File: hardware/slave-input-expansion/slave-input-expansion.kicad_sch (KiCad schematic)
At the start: 1 part

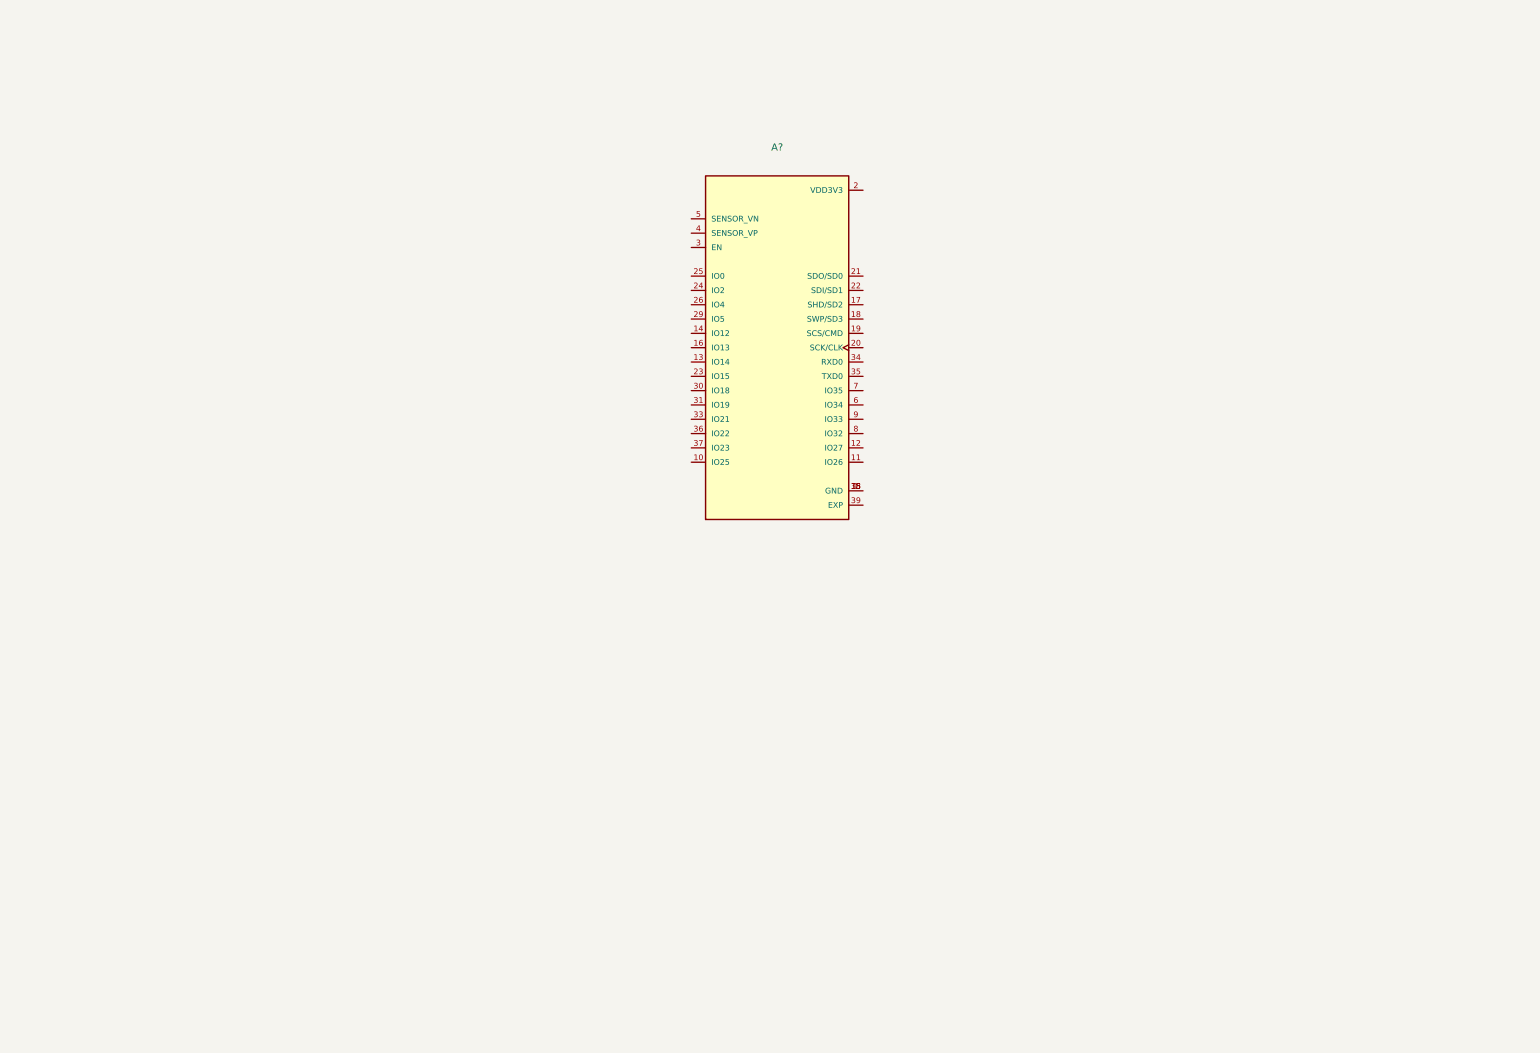
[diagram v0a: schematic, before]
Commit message: Diseños casi listos (sch)
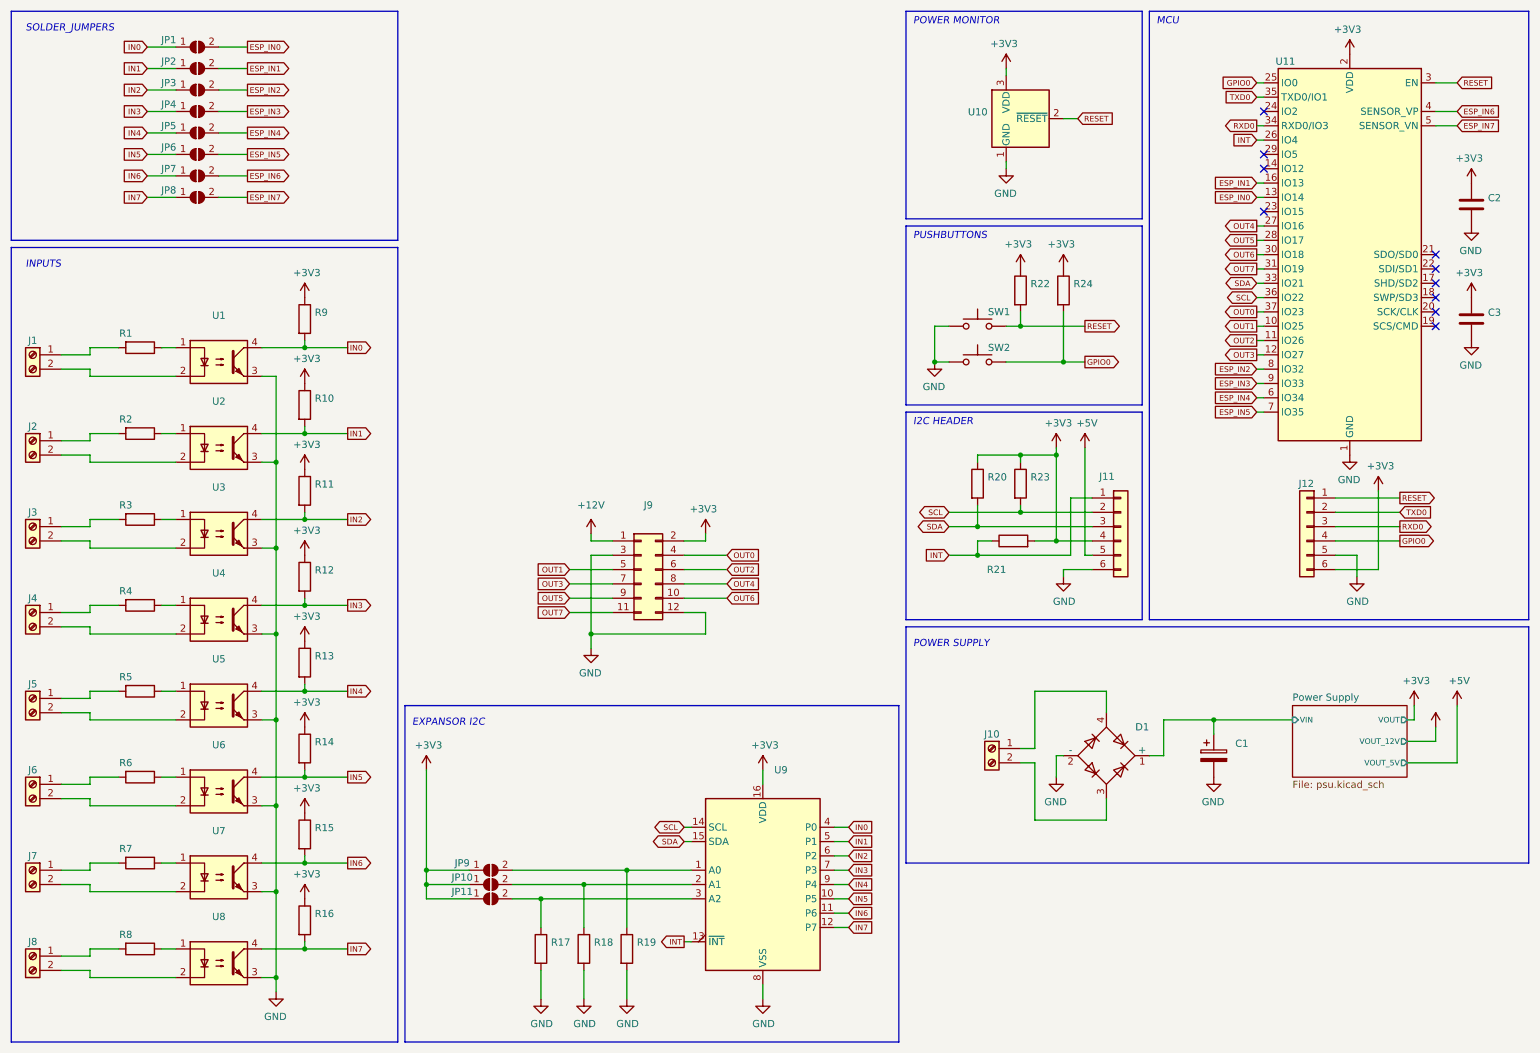
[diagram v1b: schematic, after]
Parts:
- removed A?: (no value), symbol ESP32-WROVER-I:ESP32-WROVER-I
- added C1: (no value), symbol Device:C_Polarized
- added C2, C3: (no value), symbol Device:C
- added D1: (no value), symbol Diode_Bridge:ABS10
- added J1, J10, J2, J3, J4, J5, J6, J7, J8: (no value), symbol Connector:Screw_Terminal_01x02
- added J11, J12: (no value), symbol Connector_Generic:Conn_01x06
- added J9: (no value), symbol Connector_Generic:Conn_02x06_Odd_Even
- added JP1, JP10, JP11, JP2, JP3, JP4, JP5, JP6, JP7, JP8, JP9: (no value), symbol Jumper:SolderJumper_2_Open
- added R1, R10, R11, R12, R13, R14, R15, R16, R17, R18, R19, R2, R20, R21, R22, R23, R24, R3, R4, R5, R6, R7, R8, R9: (no value), symbol Device:R
- added SW1, SW2: (no value), symbol Switch:SW_Push
- added U1, U2, U3, U4, U5, U6, U7, U8: (no value), symbol Isolator:PC817
- added U10: (no value), symbol components:DS1233
- added U11: (no value), symbol RF_Module:ESP32-WROOM-32
- added U9: (no value), symbol Interface_Expansion:PCF8574
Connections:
- new net: J7.1 (Pin_1), R7.2
- new net: J7.2 (Pin_2), U7.2
- new net: J8.1 (Pin_1), R8.2
- new net: J8.2 (Pin_2), U8.2
- new net: R5.1, U5.1
- new net: J5.2 (Pin_2), U5.2
- new net: R6.1, U6.1
- new net: J6.1 (Pin_1), R6.2
- new net: R7.1, U7.1
- new net: R2.1, U2.1
- new net: J2.2 (Pin_2), U2.2
- new net: R4.1, U4.1
- new net: J4.1 (Pin_1), R4.2
- new net: JP9.2 (B), R19.1, U9.1 (A0)
- new net: D1.3, J10.2 (Pin_2)
- new net: D1.4, J10.1 (Pin_1)
- new net: J2.1 (Pin_1), R2.2
- new net: J5.1 (Pin_1), R5.2
- new net: J6.2 (Pin_2), U6.2
- new net: J4.2 (Pin_2), U4.2
- new net: J1.1 (Pin_1), R1.2
- new net: J1.2 (Pin_2), U1.2
- new net: R1.1, U1.1
- new net: R8.1, U8.1
- new net: R3.1, U3.1
- new net: J3.1 (Pin_1), R3.2
- new net: J3.2 (Pin_2), U3.2
- new net: JP10.2 (B), R18.1, U9.2 (A1)
- new net: JP11.2 (B), R17.1, U9.3 (A2)
- new net +12V: J9.1 (Pin_1)
- new net +3V3: C2.1, C3.1, J11.4 (Pin_4), J12.6 (Pin_6), J9.2 (Pin_2), JP10.1 (A), JP11.1 (A), JP9.1 (A), R10.1, R11.1, R12.1, R13.1, R14.1, R15.1, R16.1, R20.1, R21.2, R22.1, R23.1, R24.1, R9.1, U10.3 (VDD), U11.2 (VDD), U9.16 (VDD)
- new net +5V: J11.5 (Pin_5)
- new net ESP_IN0: JP1.2 (B), U11.13 (IO14)
- new net ESP_IN1: JP2.2 (B), U11.16 (IO13)
- new net ESP_IN2: JP3.2 (B), U11.8 (IO32)
- new net ESP_IN3: JP4.2 (B), U11.9 (IO33)
- new net ESP_IN4: JP5.2 (B), U11.6 (IO34)
- new net ESP_IN5: JP6.2 (B), U11.7 (IO35)
- new net ESP_IN6: JP7.2 (B), U11.4 (SENSOR_VP)
- new net ESP_IN7: JP8.2 (B), U11.5 (SENSOR_VN)
- new net GND: C1.2, C2.2, C3.2, D1.2 (-), J11.6 (Pin_6), J12.5 (Pin_5), J9.12 (Pin_12), J9.3 (Pin_3), R17.2, R18.2, R19.2, SW1.1, SW2.1, U1.3, U10.1 (GND), U11.1 (GND), U11.15 (GND), U11.38 (GND), U11.39 (GND), U2.3, U3.3, U4.3, U5.3, U6.3, U7.3, U8.3, U9.8 (VSS)
- new net GPIO0: J12.4 (Pin_4), R24.2, SW2.2, U11.25 (IO0)
- new net IN0: JP1.1 (A), R9.2, U1.4, U9.4 (P0)
- new net IN1: JP2.1 (A), R10.2, U2.4, U9.5 (P1)
- new net IN2: JP3.1 (A), R11.2, U3.4, U9.6 (P2)
- new net IN3: JP4.1 (A), R12.2, U4.4, U9.7 (P3)
- new net IN4: JP5.1 (A), R13.2, U5.4, U9.9 (P4)
- new net IN5: JP6.1 (A), R14.2, U6.4, U9.10 (P5)
- new net IN6: JP7.1 (A), R15.2, U7.4, U9.11 (P6)
- new net IN7: JP8.1 (A), R16.2, U8.4, U9.12 (P7)
- new net INT: J11.1 (Pin_1), R21.1, U11.26 (IO4), U9.13 (~{INT})
- new net OUT0: J9.4 (Pin_4), U11.37 (IO23)
- new net OUT1: J9.5 (Pin_5), U11.10 (IO25)
- new net OUT2: J9.6 (Pin_6), U11.11 (IO26)
- new net OUT3: J9.7 (Pin_7), U11.12 (IO27)
- new net OUT4: J9.8 (Pin_8), U11.27 (IO16)
- new net OUT5: J9.9 (Pin_9), U11.28 (IO17)
- new net OUT6: J9.10 (Pin_10), U11.30 (IO18)
- new net OUT7: J9.11 (Pin_11), U11.31 (IO19)
- new net Power Supply/VIN: C1.1, D1.1 (+)
- new net RESET: J12.1 (Pin_1), R22.2, SW1.2, U10.2 (~{RESET}), U11.3 (EN)
- new net RXD0: J12.3 (Pin_3), U11.34 (RXD0/IO3)
- new net SCL: J11.2 (Pin_2), R23.2, U11.36 (IO22), U9.14 (SCL)
- new net SDA: J11.3 (Pin_3), R20.2, U11.33 (IO21), U9.15 (SDA)
- new net TXD0: J12.2 (Pin_2), U11.35 (TXD0/IO1)
- no-connect marks 0 -> 10
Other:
- added sheet Power Supply (psu.kicad_sch)
- note added: "EXPANSOR I2C"
- note added: "I2C HEADER"
- note added: "INPUTS"
- note added: "MCU"
- note added: "POWER MONITOR"
- note added: "POWER SUPPLY"
- note added: "PUSHBUTTONS"
- note added: "SOLDER_JUMPERS"

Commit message: Diseño mecanico del ensamblaje
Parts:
- C1: value (none) -> 1000uF
- C2: value (none) -> 100nF; footprint (none) -> Capacitor_SMD:C_1206_3216Metric_Pad1.33x1.80mm_HandSolder
- C3: value (none) -> 1uF; footprint (none) -> Capacitor_SMD:C_1206_3216Metric_Pad1.33x1.80mm_HandSolder
- D1: value (none) -> ABS10; footprint (none) -> Diode_SMD:Diode_Bridge_Diotec_ABS
- J1, J10, J2, J3, J4, J5, J6, J7, J8: value (none) -> Screw_Terminal_01x02; footprint (none) -> libs:TerminalBlock_bornier-2_P5.08mm
- J11: value (none) -> Conn_01x06; footprint (none) -> Connector_Molex:Molex_KK-254_AE-6410-06A_1x06_P2.54mm_Vertical
- J12: value (none) -> ICSP; footprint (none) -> Connector_PinSocket_2.54mm:PinSocket_1x06_P2.54mm_Vertical
- J9: value (none) -> Conn_02x06_Odd_Even; footprint (none) -> Connector_PinHeader_2.54mm:PinHeader_2x06_P2.54mm_Vertical
- JP1, JP10, JP11, JP2, JP3, JP4, JP5, JP6, JP7, JP8, JP9: value (none) -> SolderJumper_2_Open; footprint (none) -> Jumper:SolderJumper-2_P1.3mm_Open_RoundedPad1.0x1.5mm
- R1, R2, R3, R4, R5, R6, R7, R8: value (none) -> 2.2k; footprint (none) -> Resistor_THT:R_Axial_DIN0204_L3.6mm_D1.6mm_P5.08mm_Horizontal
- R10, R11, R12, R13, R14, R15, R16, R17, R18, R19, R20, R21, R22, R23, R24, R9: value (none) -> 10k; footprint (none) -> Resistor_SMD:R_1206_3216Metric
- SW1, SW2: value (none) -> SW_Push; footprint (none) -> Button_Switch_THT:SW_PUSH_6mm
- U1, U2, U3, U4, U5, U6, U7, U8: value (none) -> PC817XI; footprint (none) -> Package_DIP:SMDIP-4_W9.53mm
- U10: value (none) -> DS1233A-10; footprint (none) -> Package_TO_SOT_THT:TO-92
- U11: value (none) -> ESP32; footprint (none) -> esp32-wroom-roover:ESP32-WROOM-WROVER-NC
- U9: value (none) -> PCF8574; footprint (none) -> Package_SO:SOIC-16W_7.5x10.3mm_P1.27mm
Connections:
- net at J7.1 (Pin_1): now also U7.2; no longer R7.2
- net at J7.2 (Pin_2): now also R7.2; no longer U7.2
- net at J8.1 (Pin_1): now also U8.2; no longer R8.2
- net at J8.2 (Pin_2): now also R8.2; no longer U8.2
- net at U5.2: now also J5.1 (Pin_1); no longer J5.2 (Pin_2)
- net at R6.2: now also J6.2 (Pin_2); no longer J6.1 (Pin_1)
- net at U2.2: now also J2.1 (Pin_1); no longer J2.2 (Pin_2)
- net at R4.2: now also J4.2 (Pin_2); no longer J4.1 (Pin_1)
- net at R2.2: now also J2.2 (Pin_2); no longer J2.1 (Pin_1)
- net at R5.2: now also J5.2 (Pin_2); no longer J5.1 (Pin_1)
- net at U6.2: now also J6.1 (Pin_1); no longer J6.2 (Pin_2)
- net at U4.2: now also J4.1 (Pin_1); no longer J4.2 (Pin_2)
- net at J1.1 (Pin_1): now also U1.2; no longer R1.2
- net at J1.2 (Pin_2): now also R1.2; no longer U1.2
- net at R3.2: now also J3.2 (Pin_2); no longer J3.1 (Pin_1)
- net at U3.2: now also J3.1 (Pin_1); no longer J3.2 (Pin_2)
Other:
- moved on the sheet: J1, J2, J3, J4, J5, J6, J7, J8

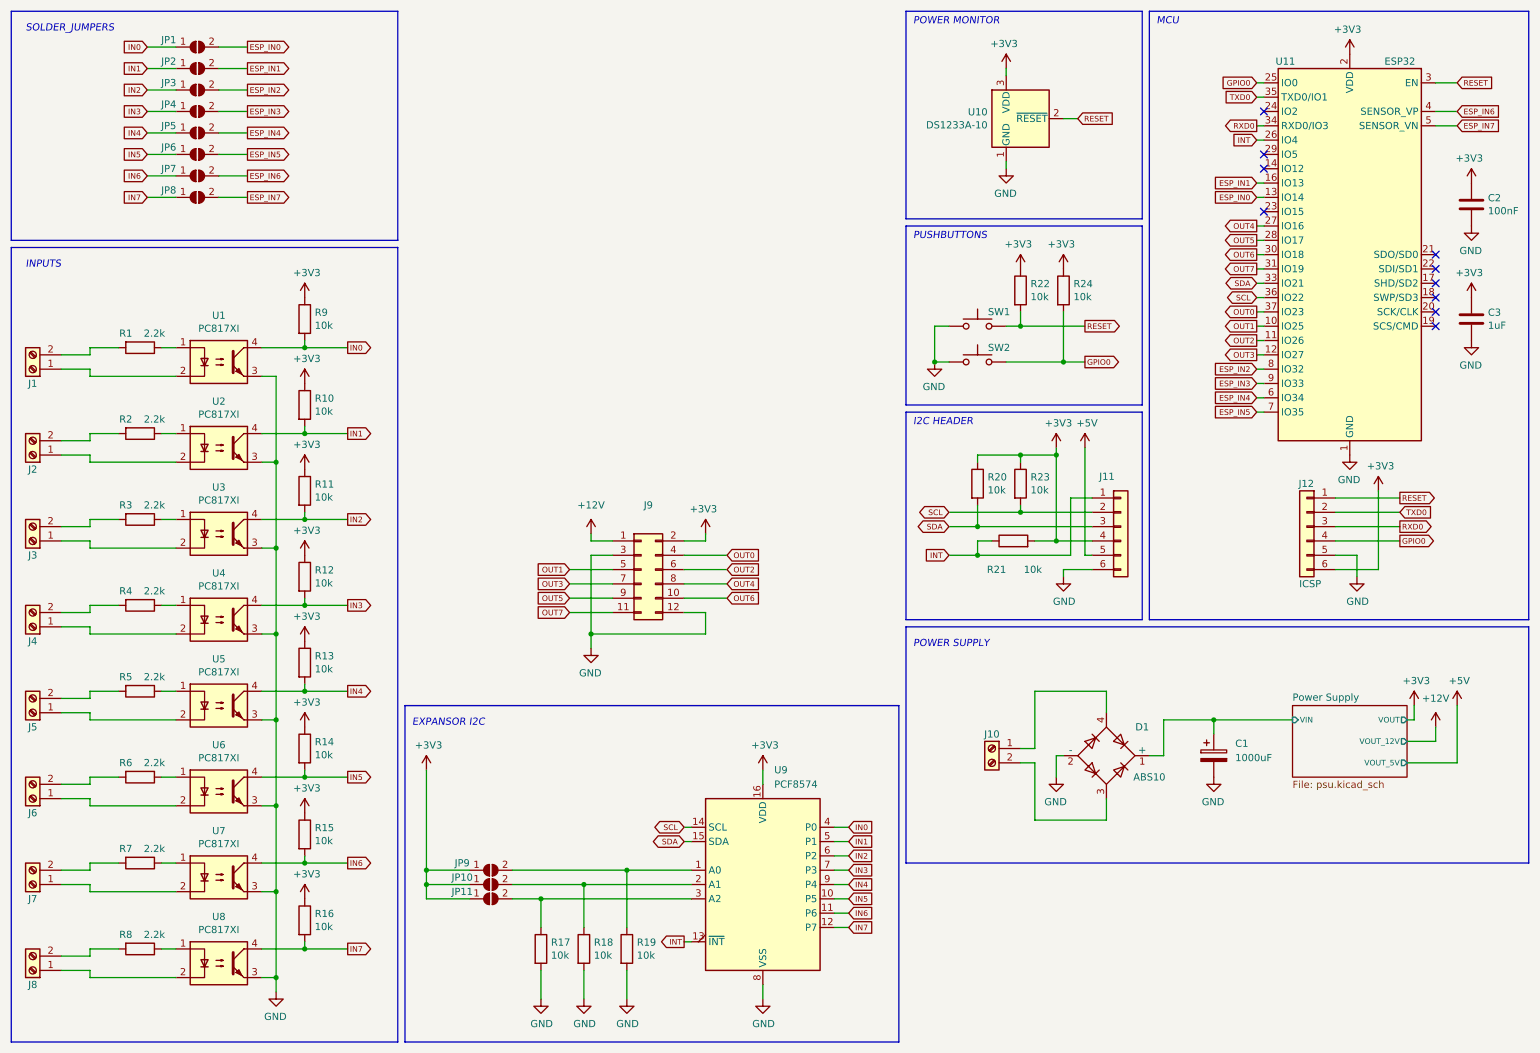
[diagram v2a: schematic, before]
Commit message: Routeo de la placa expansion
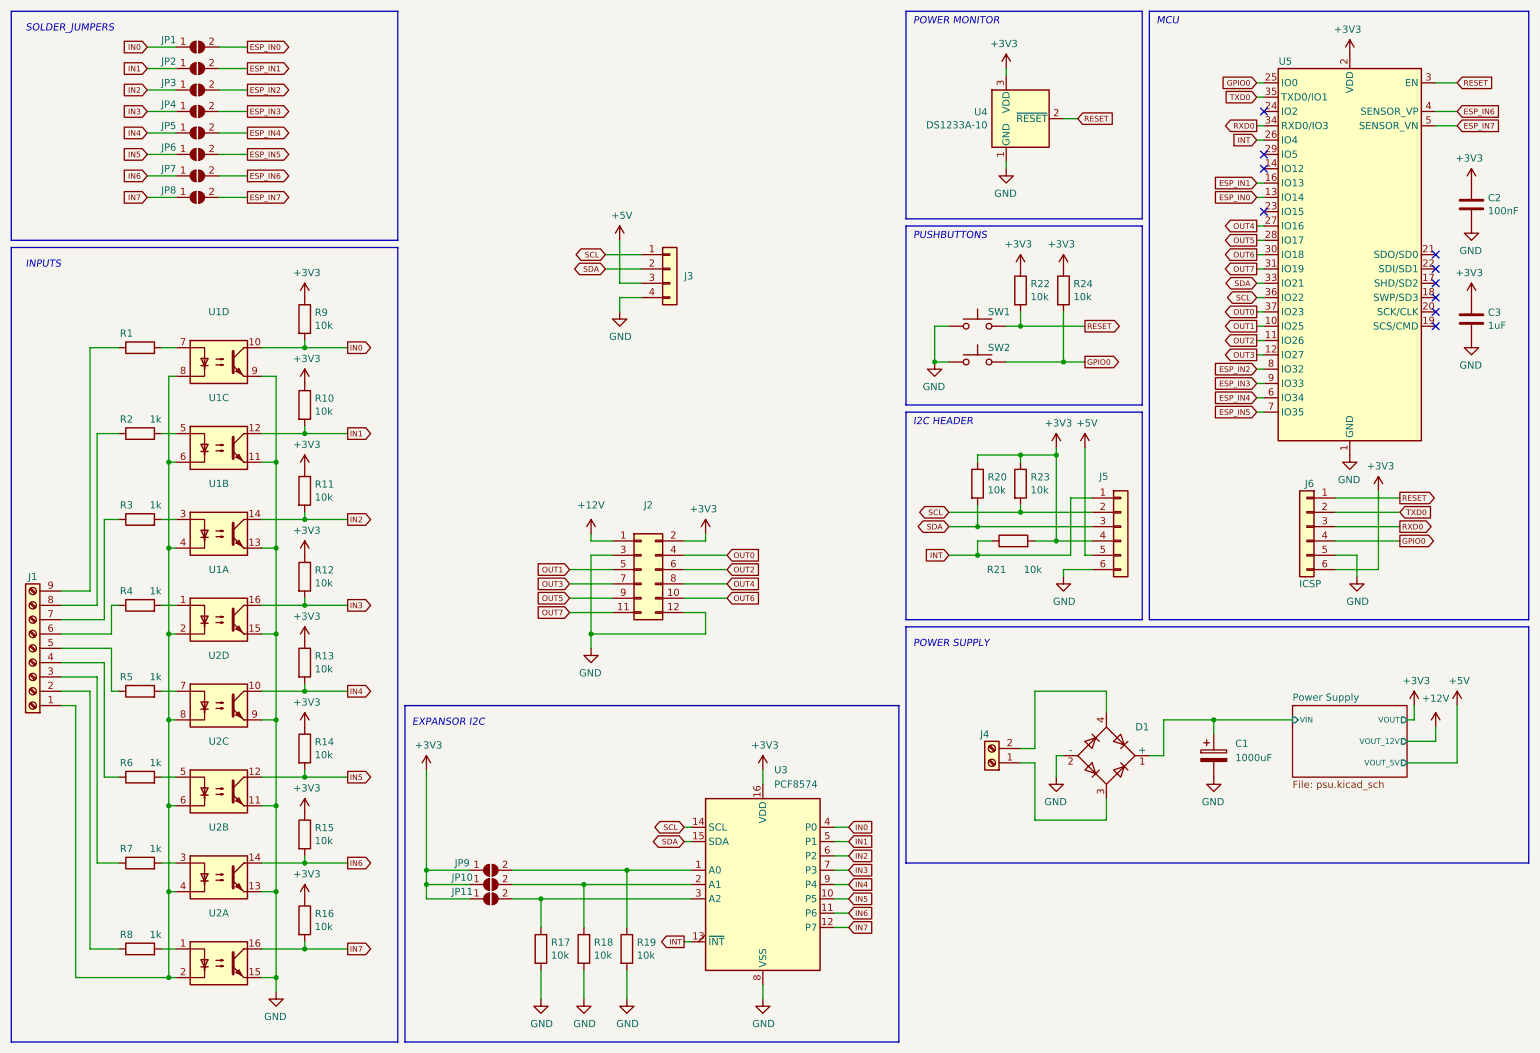
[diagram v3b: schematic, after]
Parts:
- removed J1, J2, J3, J4, J5, J6, J7, J8: Screw_Terminal_01x02, libs:TerminalBlock_bornier-2_P5.08mm, symbol Connector:Screw_Terminal_01x02
- removed U1, U2, U3, U4, U5, U6, U7, U8: PC817XI, Package_DIP:SMDIP-4_W9.53mm, symbol Isolator:PC817
- added J1: (no value), symbol Connector:Screw_Terminal_01x09
- added J3: (no value), symbol Connector_Generic:Conn_01x04
- added U1, U2: (no value), symbol Isolator:LTV-847S
- D1: value ABS10 -> (none); footprint Diode_SMD:Diode_Bridge_Diotec_ABS -> (none)
- J4: renamed from J10; value Screw_Terminal_01x02 -> (none); footprint libs:TerminalBlock_bornier-2_P5.08mm -> (none)
- R1: value 2.2k -> (none); footprint Resistor_THT:R_Axial_DIN0204_L3.6mm_D1.6mm_P5.08mm_Horizontal -> (none); manf# (none) -> RC1206FR-071KL
- R2, R3, R4, R5, R6, R7, R8: value 2.2k -> 1k; footprint Resistor_THT:R_Axial_DIN0204_L3.6mm_D1.6mm_P5.08mm_Horizontal -> Resistor_SMD:R_1206_3216Metric; manf# (none) -> RC1206FR-071KL
- U5: renamed from U11; value ESP32 -> (none); footprint esp32-wroom-roover:ESP32-WROOM-WROVER-NC -> (none)
- renumbered J9 to J2, J11 to J5, J12 to J6, U9 to U3, U10 to U4
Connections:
- net +5V: now also J3.3 (Pin_3)
- net GND: now also J3.4 (Pin_4), U1.11, U1.13, U1.15, U1.9, U2.11, U2.13, U2.15, U2.9
- net IN0: now also U1.10
- net IN1: now also U1.12
- net IN2: now also U1.14
- net IN3: now also U1.16
- net IN4: now also U2.10
- net IN5: now also U2.12
- net IN6: now also U2.14
- net IN7: now also U2.16
- net SCL: now also J3.1 (Pin_1)
- net SDA: now also J3.2 (Pin_2)
- net at R7.2: now also U2.3
- net at R8.2: now also U2.1
- net at R5.1: now also J1.5 (Pin_5)
- net at R6.1: now also J1.4 (Pin_4)
- net at R6.2: now also U2.5
- net at R7.1: now also J1.3 (Pin_3)
- net at R2.1: now also J1.8 (Pin_8)
- net at R4.1: now also J1.6 (Pin_6)
- net at R4.2: now also U1.1
- net at D1.3: now also J4.1 (Pin_1); no longer J4.2 (Pin_2)
- net at D1.4: now also J4.2 (Pin_2); no longer J4.1 (Pin_1)
- net at R2.2: now also U1.5
- net at R5.2: now also U2.7
- net at R1.2: now also U1.7
- net at R1.1: now also J1.9 (Pin_9)
- net at R8.1: now also J1.2 (Pin_2)
- net at R3.1: now also J1.7 (Pin_7)
- net at R3.2: now also U1.3
- new net: J1.1 (Pin_1), U1.2, U1.4, U1.6, U1.8, U2.2, U2.4, U2.6, U2.8
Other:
- moved on the sheet: J4
